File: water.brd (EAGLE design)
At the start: 100 x 80 mm, 15 parts, among them K1 AQH2223, K2 AQH2223, K3 AQH2223, K4 AQH2223, X5 MKDSN1,5/2-5,08, X6 MKDSN1,5/2-5,08, X7 MKDSN1,5/2-5,08, X8 MKDSN1,5/2-5,08

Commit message: Changes
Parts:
- moved X8 77.9 mm to (42.7, 46.3)
- moved D1 76.8 mm to (8.63, 46.0)
- moved X5 67.6 mm to (18.4, 38.1)
- moved X7 54.1 mm to (33.7, 37.3)
- moved K2 4.12 mm to (44.3, 23.9)
- moved K3 4.12 mm to (44.3, 9.16)
- moved U2 3.16 mm to (11.0, 14.2)
- moved K1 2.24 mm to (33.6, 23.9)
- moved K4 2.24 mm to (33.6, 9.16)
- moved R1 2.00 mm to (24.7, 14.0)
- moved R2 2.00 mm to (24.7, 10.2)
- moved R3 2.00 mm to (24.7, 3.81)
- moved R4 2.00 mm to (24.7, 19.1)
- moved X6 1.41 mm to (29.5, 46.0)
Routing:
- net GND: track 0.00 -> 117.8 mm
- net N$9: track 0.00 -> 37.6 mm
- net N$10: track 0.00 -> 36.3 mm
- net +3V3: track 0.00 -> 34.4 mm, vias 0 -> 1
- net N$8: track 0.00 -> 27.5 mm
- net N$15: track 0.00 -> 25.8 mm
- net N$2: track 0.00 -> 19.4 mm
- net N$3: track 0.00 -> 19.0 mm
- net N$11: track 0.00 -> 13.5 mm
- net N$12: track 0.00 -> 11.2 mm
- net N$14: track 0.00 -> 10.6 mm
- net N$1: track 0.00 -> 7.11 mm
- net N$4: track 0.00 -> 6.83 mm
- net N$5: track 0.00 -> 5.42 mm
- net N$7: track 0.00 -> 4.23 mm
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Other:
- board size 100 x 80 mm -> 62.7 x 68 mm

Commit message: Move parts
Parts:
- added SV2: (no value), con-lstb:MA04-2
- R1, R2, R3, R4: value 220 -> (none)
- moved D1 15.8 mm to (21.6, 37.0)
- moved X5 13.3 mm to (7.00, 45.0)
- moved K3 12.4 mm to (32.0, 7.00)
- moved X6 10.5 mm to (19.0, 45.0)
- moved K4 9.68 mm to (43.0, 7.00)
- moved X7 8.16 mm to (31.0, 45.0)
- moved K1 5.10 mm to (32.0, 19.0)
- moved K2 5.02 mm to (43.0, 19.0)
- moved SV1 3.16 mm to (3.35, 34.6), turned to 270 degrees
- moved X8 1.32 mm to (43.0, 45.0)
- moved R1 1.23 mm to (24.0, 15.0)
- moved R4 1.16 mm to (24.0, 20.0)
- moved R3 0.70 mm to (24.0, 4.00)
- moved R2 0.69 mm to (24.0, 10.0)
- moved U2 0.24 mm to (11.0, 14.0)
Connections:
- new net N$13: SV2.8, U2.CH_PD
- new net N$16: SV2.6, U2.RESET
- new net N$17: SV2.3, U2.TXD0
- new net N$18: SV2.1, U2.RXD0
- new net N$19: SV2.4, U2.GPIO15
- new net N$20: SV2.2, U2.GPIO0
- net +3V3: now also SV2.7
- net GND: now also SV2.5
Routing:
- net GND: track 117.8 -> 0.00 mm
- net N$9: track 37.6 -> 0.00 mm
- net N$10: track 36.3 -> 0.00 mm
- net +3V3: track 34.4 -> 0.00 mm, vias 1 -> 0
- net N$8: track 27.5 -> 0.00 mm
- net N$15: track 25.8 -> 0.00 mm
- net N$2: track 19.4 -> 0.00 mm
- net N$3: track 19.0 -> 0.00 mm
- net N$11: track 13.5 -> 0.00 mm
- net N$12: track 11.2 -> 0.00 mm
- net N$14: track 10.6 -> 0.00 mm
- net N$1: track 7.11 -> 0.00 mm
- net N$4: track 6.83 -> 0.00 mm
- net N$5: track 5.42 -> 0.00 mm
- net N$7: track 4.23 -> 0.00 mm
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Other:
- board size 62.7 x 68 mm -> 50 x 50 mm

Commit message: Restart routing
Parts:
- moved K1 1.00 mm to (32.0, 20.0)
- moved K2 1.00 mm to (43.0, 20.0)
- moved K3 1.00 mm to (32.0, 8.00)
- moved K4 1.00 mm to (43.0, 8.00)
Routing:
- net GND: track 0.00 -> 81.4 mm
- net N$10: track 0.00 -> 51.0 mm
- net N$12: track 0.00 -> 47.0 mm
- net N$9: track 0.00 -> 37.8 mm
- net N$11: track 0.00 -> 33.2 mm
- net N$4: track 0.00 -> 19.9 mm
- net N$2: track 0.00 -> 18.5 mm
- net N$3: track 0.00 -> 8.93 mm
- net N$1: track 0.00 -> 7.52 mm
- net N$5: track 0.00 -> 6.64 mm
- net N$6: track 0.00 -> 3.98 mm
- net N$7: track 0.00 -> 3.56 mm

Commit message: Changes
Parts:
- added C1, C2: 470uf, resistor:E5-10,5
- moved SV1 34.0 mm to (37.4, 34.6), turned to 90 degrees
- moved D1 20.2 mm to (41.6, 34.0), turned to 90 degrees
- moved SV2 6.00 mm to (5.00, 35.0)
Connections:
- new net N$21: K1.8, K2.8, K3.8, K4.8, X5.1
- net +3V3: now also C1.+, C2.+
- net GND: now also C1.-, C2.-; no longer K1.8, K2.8, K3.8, K4.8, X5.1
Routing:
- net N$21: track 0.00 -> 112.7 mm
- net +3V3: track 0.00 -> 66.9 mm
- net GND: track 81.4 -> 122.8 mm
- net N$15: track 0.00 -> 34.6 mm
- net N$18: track 0.00 -> 20.7 mm
- net N$17: track 0.00 -> 20.4 mm
- net N$14: track 0.00 -> 5.55 mm

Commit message: Changes
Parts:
- added LED1, LED2, LED3: X42180, led:Z-POWER-LED-DOME-TYPE
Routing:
- net N$19: track 0.00 -> 33.6 mm
- net N$13: track 0.00 -> 26.7 mm
- net N$20: track 0.00 -> 26.1 mm
- net N$8: track 0.00 -> 21.5 mm
- net N$16: track 0.00 -> 17.5 mm
- net N$18: track 20.7 -> 19.0 mm
- net N$17: track 20.4 -> 19.3 mm
- net +3V3: track 66.9 -> 66.7 mm, vias 0 -> 1
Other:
- board text added: "Sebastian Boyd"
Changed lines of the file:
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@@
 <wire x1="50" y1="50" x2="0" y2="50" width="0" layer="20"/>
 <wire x1="0" y1="50" x2="0" y2="0" width="0" layer="20"/>
+<text x="48" y="2" size="1.778" layer="16" rot="MR0">Sebastian Boyd</text>
 </plain>
 <attributes>
@@
 <element name="C1" library="resistor" library_urn="urn:adsk.eagle:library:348" package="E5-10,5" value="470uf" x="28" y="35" rot="R270"/>
 <element name="C2" library="resistor" library_urn="urn:adsk.eagle:library:348" package="E5-10,5" value="470uf" x="16" y="35" rot="R270"/>
+<element name="LED1" library="led" library_urn="urn:adsk.eagle:library:259" package="Z-POWER-LED-DOME-TYPE" value="X42180" x="7" y="-9"/>
+<element name="LED2" library="led" library_urn="urn:adsk.eagle:library:259" package="Z-POWER-LED-DOME-TYPE" value="X42180" x="7" y="-22"/>
+<element name="LED3" library="led" library_urn="urn:adsk.eagle:library:259" package="Z-POWER-LED-DOME-TYPE" value="X42180" x="7" y="-35"/>
 </elements>
 <signals>
@@
 <contactref element="U2" pad="GPIO13"/>
 <contactref element="R3" pad="1"/>
-<wire x1="2.7" y1="7.8" x2="22.578" y2="4" width="0" layer="19" extent="1-1"/>
+<wire x1="18.288" y1="4.1148" x2="22.5552" y2="4.1148" width="0.1524" layer="1"/>
+<wire x1="14.6304" y1="7.7724" x2="18.288" y2="4.1148" width="0.1524" layer="1"/>
+<wire x1="2.7432" y1="7.7724" x2="14.6304" y2="7.7724" width="0.1524" layer="1"/>
+<wire x1="22.5552" y1="4.1148" x2="22.578" y2="4" width="0.1524" layer="1"/>
+<wire x1="2.7432" y1="7.7724" x2="2.7" y2="7.8" width="0.1524" layer="1"/>
 </signal>
 <signal name="N$9">
@@
 <wire x1="16" y1="37.54" x2="7.54" y2="37.54" width="0.4064" layer="1"/>
 <wire x1="6.27" y1="38.81" x2="7.54" y2="37.54" width="0.4064" layer="1"/>
-<wire x1="2.7" y1="5.8" x2="3.8" y2="5.8" width="0.1524" layer="1"/>
-<wire x1="3.8" y1="5.8" x2="5" y2="7" width="0.1524" layer="1"/>
-<wire x1="5" y1="7" x2="5" y2="37.54" width="0.1524" layer="1"/>
-<wire x1="5" y1="37.54" x2="6.27" y2="38.81" width="0.1524" layer="1"/>
+<wire x1="3.5052" y1="5.9436" x2="2.7432" y2="5.9436" width="0.1524" layer="1"/>
+<wire x1="4.7244" y1="7.1628" x2="3.5052" y2="5.9436" width="0.1524" layer="1"/>
+<wire x1="4.7244" y1="37.1856" x2="4.7244" y2="7.1628" width="0.1524" layer="16"/>
+<wire x1="6.2484" y1="38.7096" x2="4.7244" y2="37.1856" width="0.1524" layer="16"/>
+<wire x1="2.7432" y1="5.9436" x2="2.7" y2="5.8" width="0.1524" layer="1"/>
+<wire x1="6.2484" y1="38.7096" x2="6.27" y2="38.81" width="0.1524" layer="16"/>
+<via x="4.7244" y="7.1628" extent="1-16" drill="0.3048"/>
 </signal>
 <signal name="N$15">
@@
 <contactref element="SV2" pad="8"/>
 <contactref element="U2" pad="CH_PD"/>
-<wire x1="2.7" y1="15.8" x2="3.73" y2="38.81" width="0" layer="19" extent="1-1"/>
+<wire x1="3.2004" y1="15.8496" x2="2.7432" y2="15.8496" width="0.1524" layer="1"/>
+<wire x1="4.572" y1="17.2212" x2="3.2004" y2="15.8496" width="0.1524" layer="1"/>
+<wire x1="4.572" y1="28.3464" x2="4.572" y2="17.2212" width="0.1524" layer="1"/>
+<wire x1="2.286" y1="30.6324" x2="4.572" y2="28.3464" width="0.1524" layer="1"/>
+<wire x1="2.286" y1="33.8328" x2="2.286" y2="30.6324" width="0.1524" layer="1"/>
+<wire x1="3.6576" y1="35.2044" x2="2.286" y2="33.8328" width="0.1524" layer="1"/>
+<wire x1="4.1148" y1="35.2044" x2="3.6576" y2="35.2044" width="0.1524" layer="1"/>
+<wire x1="4.7244" y1="35.814" x2="4.1148" y2="35.2044" width="0.1524" layer="1"/>
+<wire x1="4.7244" y1="37.7952" x2="4.7244" y2="35.814" width="0.1524" layer="1"/>
+<wire x1="3.81" y1="38.7096" x2="4.7244" y2="37.7952" width="0.1524" layer="1"/>
+<wire x1="2.7432" y1="15.8496" x2="2.7" y2="15.8" width="0.1524" layer="1"/>
+<wire x1="3.81" y1="38.7096" x2="3.73" y2="38.81" width="0.1524" layer="1"/>
 </signal>
 <signal name="N$16">
 <contactref element="U2" pad="RESET"/>
 <contactref element="SV2" pad="6"/>
-<wire x1="2.7" y1="19.8" x2="3.73" y2="36.27" width="0" layer="19" extent="1-1"/>
+<wire x1="2.5908" y1="29.8704" x2="2.5908" y2="19.812" width="0.1524" layer="1"/>
+<wire x1="1.9812" y1="30.48" x2="2.5908" y2="29.8704" width="0.1524" layer="1"/>
+<wire x1="1.9812" y1="34.4424" x2="1.9812" y2="30.48" width="0.1524" layer="1"/>
+<wire x1="3.6576" y1="36.1188" x2="1.9812" y2="34.4424" width="0.1524" layer="1"/>
+<wire x1="2.5908" y1="19.812" x2="2.7" y2="19.8" width="0.1524" layer="1"/>
+<wire x1="3.6576" y1="36.1188" x2="3.73" y2="36.27" width="0.1524" layer="1"/>
 </signal>
 <signal name="N$17">
 <contactref element="U2" pad="TXD0"/>
 <contactref element="SV2" pad="3"/>
-<wire x1="6.27" y1="33.73" x2="8.27" y2="33.73" width="0.1524" layer="1"/>
-<wire x1="8.27" y1="33.73" x2="19" y2="23" width="0.1524" layer="1"/>
-<wire x1="19" y1="23" x2="19" y2="19.9" width="0.1524" layer="1"/>
-<wire x1="19" y1="19.9" x2="19.1" y2="19.8" width="0.1524" layer="1"/>
+<wire x1="19.05" y1="21.0312" x2="19.05" y2="19.812" width="0.1524" layer="1"/>
+<wire x1="6.4008" y1="33.6804" x2="19.05" y2="21.0312" width="0.1524" layer="1"/>
+<wire x1="19.05" y1="19.812" x2="19.1" y2="19.8" width="0.1524" layer="1"/>
+<wire x1="6.4008" y1="33.6804" x2="6.27" y2="33.73" width="0.1524" layer="1"/>
 </signal>
 <signal name="N$18">
 <contactref element="U2" pad="RXD0"/>
 <contactref element="SV2" pad="1"/>
-<wire x1="6.27" y1="31.19" x2="8.81" y2="31.19" width="0.1524" layer="1"/>
-<wire x1="8.81" y1="31.19" x2="17" y2="23" width="0.1524" layer="1"/>
-<wire x1="17" y1="23" x2="17" y2="19" width="0.1524" layer="1"/>
-<wire x1="17" y1="19" x2="18" y2="18" width="0.1524" layer="1"/>
-<wire x1="18" y1="18" x2="18.9" y2="18" width="0.1524" layer="1"/>
-<wire x1="18.9" y1="18" x2="19.1" y2="17.8" width="0.1524" layer="1"/>
+<wire x1="18.5928" y1="17.8308" x2="19.05" y2="17.8308" width="0.1524" layer="1"/>
+<wire x1="6.4008" y1="30.0228" x2="18.5928" y2="17.8308" width="0.1524" layer="1"/>
+<wire x1="6.4008" y1="31.0896" x2="6.4008" y2="30.0228" width="0.1524" layer="1"/>
+<wire x1="19.05" y1="17.8308" x2="19.1" y2="17.8" width="0.1524" layer="1"/>
+<wire x1="6.4008" y1="31.0896" x2="6.27" y2="31.19" width="0.1524" layer="1"/>
 </signal>
 <signal name="N$19">
 <contactref element="SV2" pad="4"/>
 <contactref element="U2" pad="GPIO15"/>
-<wire x1="19.1" y1="7.8" x2="3.73" y2="33.73" width="0" layer="19" extent="1-1"/>
+<wire x1="18.4404" y1="7.9248" x2="19.05" y2="7.9248" width="0.1524" layer="1"/>
+<wire x1="4.8768" y1="21.4884" x2="18.4404" y2="7.9248" width="0.1524" layer="1"/>
+<wire x1="4.8768" y1="28.4988" x2="4.8768" y2="21.4884" width="0.1524" layer="1"/>
+<wire x1="2.5908" y1="30.7848" x2="4.8768" y2="28.4988" width="0.1524" layer="1"/>
+<wire x1="2.5908" y1="32.6136" x2="2.5908" y2="30.7848" width="0.1524" layer="1"/>
+<wire x1="3.6576" y1="33.6804" x2="2.5908" y2="32.6136" width="0.1524" layer="1"/>
+<wire x1="19.05" y1="7.9248" x2="19.1" y2="7.8" width="0.1524" layer="1"/>
+<wire x1="3.6576" y1="33.6804" x2="3.73" y2="33.73" width="0.1524" layer="1"/>
 </signal>
 <signal name="N$20">
 <contactref element="U2" pad="GPIO0"/>
 <contactref element="SV2" pad="2"/>
-<wire x1="19.1" y1="11.8" x2="3.73" y2="31.19" width="0" layer="19" extent="1-1"/>
+<wire x1="18.4404" y1="11.8872" x2="19.05" y2="11.8872" width="0.1524" layer="1"/>
+<wire x1="5.1816" y1="25.146" x2="18.4404" y2="11.8872" width="0.1524" layer="1"/>
+<wire x1="5.1816" y1="29.718" x2="5.1816" y2="25.146" width="0.1524" layer="1"/>
+<wire x1="3.81" y1="31.0896" x2="5.1816" y2="29.718" width="0.1524" layer="1"/>
+<wire x1="19.05" y1="11.8872" x2="19.1" y2="11.8" width="0.1524" layer="1"/>
+<wire x1="3.81" y1="31.0896" x2="3.73" y2="31.19" width="0.1524" layer="1"/>
 </signal>
 <signal name="N$21">

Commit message: Add led
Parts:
- removed LED2, LED3: X42180, led:Z-POWER-LED-DOME-TYPE
- added R5: (no value), resistor:R1206
- moved LED1 45.7 mm to (25.0, 33.0), flipped to the bottom
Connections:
- new net N$22: LED1.A, R5.1
- net +3V3: now also R5.2
- net GND: now also LED1.C
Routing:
- net +3V3: track 66.7 -> 77.6 mm
- net N$22: track 0.00 -> 7.30 mm
- net GND: track 122.8 -> 125.9 mm
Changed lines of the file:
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@@
 <element name="C1" library="resistor" library_urn="urn:adsk.eagle:library:348" package="E5-10,5" value="470uf" x="28" y="35" rot="R270"/>
 <element name="C2" library="resistor" library_urn="urn:adsk.eagle:library:348" package="E5-10,5" value="470uf" x="16" y="35" rot="R270"/>
-<element name="LED1" library="led" library_urn="urn:adsk.eagle:library:259" package="Z-POWER-LED-DOME-TYPE" value="X42180" x="7" y="-9"/>
-<element name="LED2" library="led" library_urn="urn:adsk.eagle:library:259" package="Z-POWER-LED-DOME-TYPE" value="X42180" x="7" y="-22"/>
-<element name="LED3" library="led" library_urn="urn:adsk.eagle:library:259" package="Z-POWER-LED-DOME-TYPE" value="X42180" x="7" y="-35"/>
+<element name="LED1" library="led" library_urn="urn:adsk.eagle:library:259" package="Z-POWER-LED-DOME-TYPE" value="X42180" x="25" y="33" rot="MR0"/>
+<element name="R5" library="resistor" library_urn="urn:adsk.eagle:library:348" package="R1206" value="" x="37" y="28" rot="MR180"/>
 </elements>
 <signals>
@@
 <wire x1="24" y1="28.46" x2="28" y2="32.46" width="0.4064" layer="1"/>
 <wire x1="24" y1="18" x2="24" y2="28.46" width="0.4064" layer="1"/>
+<contactref element="LED1" pad="C"/>
+<wire x1="16.1444" y1="32.83443125" x2="16.1444" y2="32.6044" width="0.4064" layer="16"/>
+<wire x1="16.1444" y1="32.6044" x2="16" y2="32.46" width="0.4064" layer="16"/>
+<wire x1="18.35" y1="34.12" x2="17.42996875" y2="34.12" width="0.4064" layer="16"/>
+<wire x1="17.42996875" y1="34.12" x2="16.1444" y2="32.83443125" width="0.4064" layer="16"/>
 </signal>
 <signal name="N$5">
@@
 <wire x1="6.2484" y1="38.7096" x2="6.27" y2="38.81" width="0.1524" layer="16"/>
 <via x="4.7244" y="7.1628" extent="1-16" drill="0.3048"/>
+<contactref element="R5" pad="2"/>
+<wire x1="38.422" y1="28" x2="38.422" y2="29.422" width="0.4064" layer="16"/>
+<wire x1="38.422" y1="29.422" x2="40" y2="31" width="0.4064" layer="16"/>
+<wire x1="40" y1="31" x2="40" y2="34.45" width="0.4064" layer="16"/>
+<wire x1="40" y1="34.45" x2="37.35" y2="37.1" width="0.4064" layer="16"/>
 </signal>
 <signal name="N$15">
@@
 <wire x1="29.1996" y1="17.26219375" x2="28.19" y2="18.27179375" width="0.4064" layer="16"/>
 </signal>
+<signal name="N$22">
+<contactref element="LED1" pad="A"/>
+<contactref element="R5" pad="1"/>
+<wire x1="31.65" y1="31.88" x2="34.12" y2="31.88" width="0.4064" layer="16"/>
+<wire x1="34.12" y1="31.88" x2="36" y2="30" width="0.4064" layer="16"/>
+<wire x1="36" y1="30" x2="36" y2="28.422" width="0.4064" layer="16"/>
+<wire x1="36" y1="28.422" x2="35.578" y2="28" width="0.4064" layer="16"/>
+</signal>
 </signals>

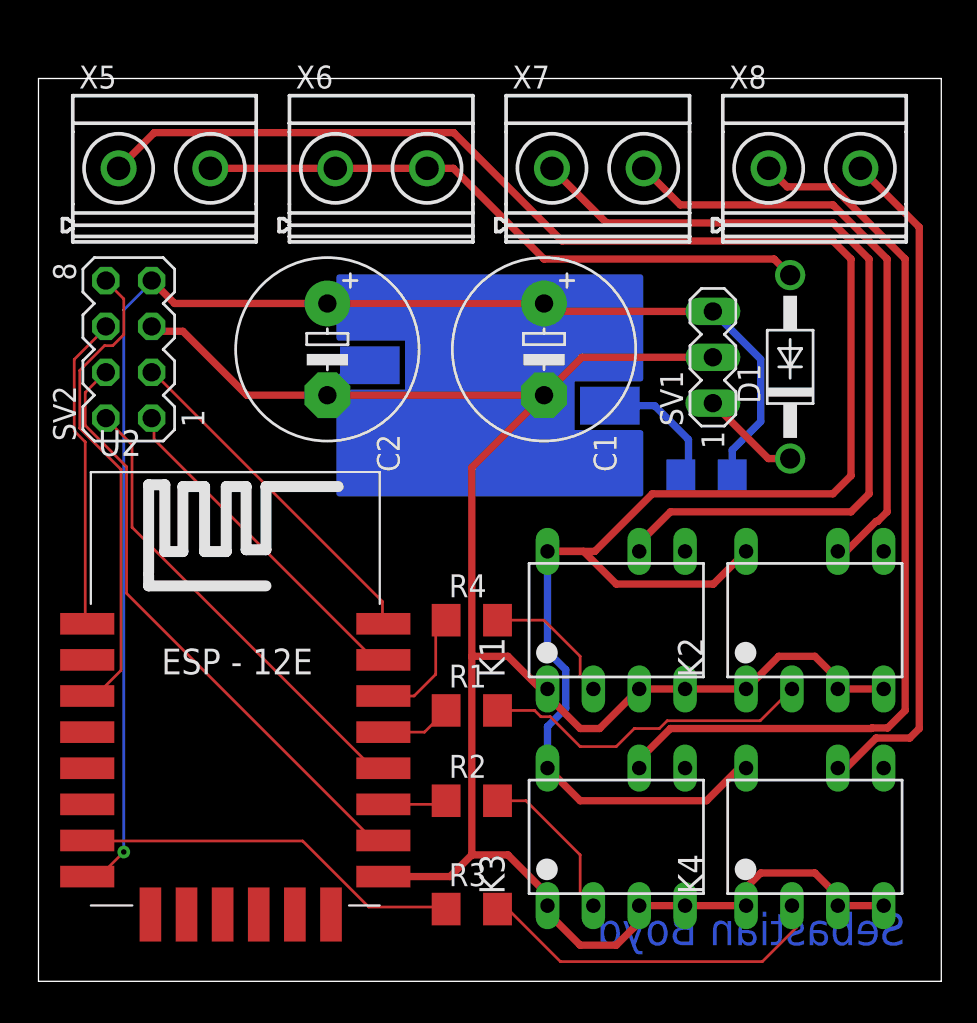
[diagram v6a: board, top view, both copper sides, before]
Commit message: Add pogo test bed
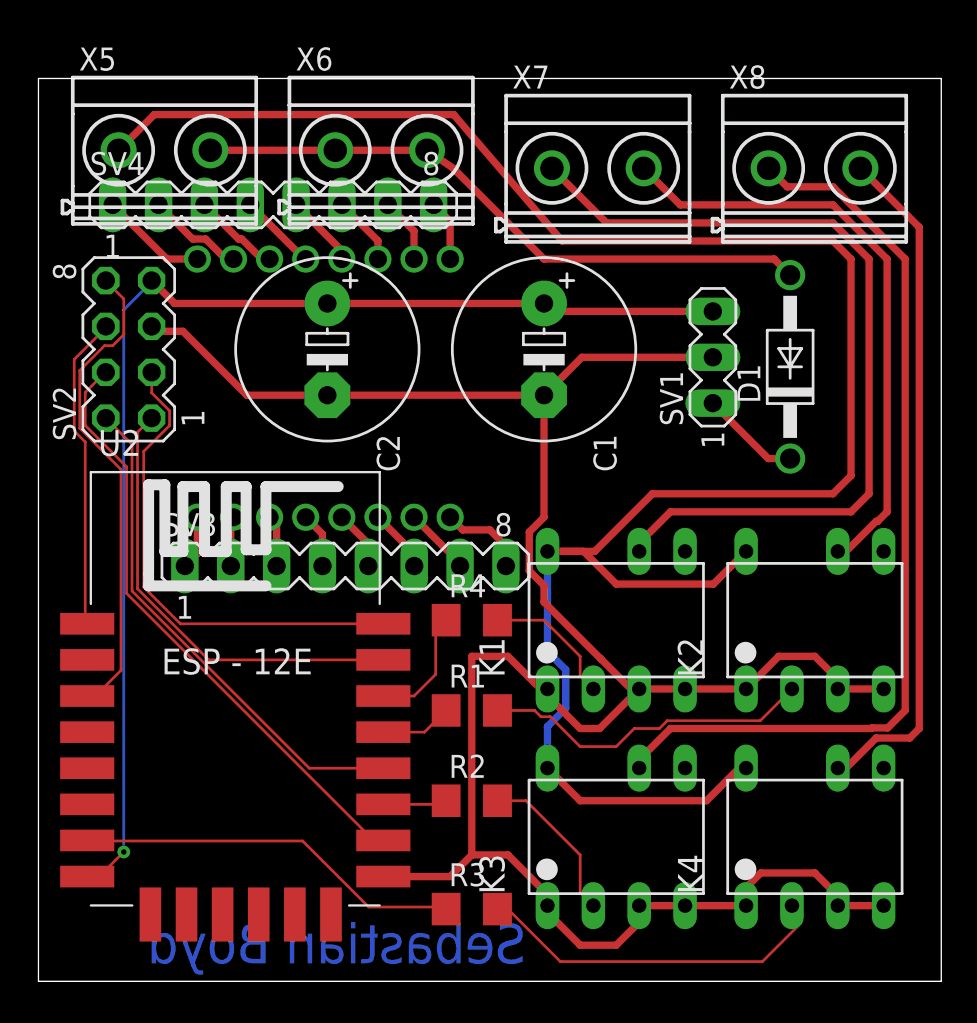
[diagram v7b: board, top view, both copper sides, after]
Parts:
- removed LED1: X42180, led:Z-POWER-LED-DOME-TYPE
- removed R5: (no value), resistor:R1206
- added SV3, SV4: (no value), con-lstb:MA08-1
- added U1: (no value), my-parts:ESP12E-POGO
- moved X5 1.00 mm to (7.00, 46.0)
- moved X6 1.00 mm to (19.0, 46.0)
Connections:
- new net N$23: SV3.2, U1.GPIO13
- new net N$24: SV3.3, U1.GPIO12
- new net N$25: SV3.4, U1.GPIO14
- new net N$26: SV3.5, U1.GPIO16
- new net N$27: SV3.6, U1.CH_PD
- new net N$28: SV3.7, U1.ADC
- new net N$29: SV3.8, U1.RESET
- new net N$30: SV4.1, U1.GND
- new net N$31: SV4.2, U1.GPIO15
- new net N$32: SV4.3, U1.GPIO2
- new net N$33: SV4.4, U1.GPIO0
- new net N$34: SV4.5, U1.GPIO4
- new net N$35: SV4.6, U1.GPIO5
- new net N$36: SV4.7, U1.RXD0
- new net N$37: SV4.8, U1.TXD0
- net +3V3: no longer R5.2
- net GND: no longer LED1.C
- net N$22: now also SV3.1, U1.VCC; no longer LED1.A, R5.1
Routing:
- net +3V3: track 77.6 -> 66.7 mm
- net N$17: track 19.3 -> 27.0 mm
- net N$18: track 19.0 -> 25.0 mm
- net N$30: track 0.00 -> 5.93 mm
- net N$31: track 0.00 -> 5.39 mm
- net N$29: track 0.00 -> 4.86 mm
- net N$32: track 0.00 -> 4.85 mm
- net N$22: track 7.30 -> 2.99 mm
- net N$33: track 0.00 -> 4.31 mm
- net N$34: track 0.00 -> 4.05 mm
- net N$35: track 0.00 -> 3.82 mm
- net N$28: track 0.00 -> 3.76 mm
- net N$36: track 0.00 -> 3.60 mm
- net N$27: track 0.00 -> 3.53 mm
- net N$37: track 0.00 -> 3.38 mm
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
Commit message: More features
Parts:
- removed SV1: (no value), con-lstb:MA03-1
- added D2: 1N4004, diode:DO41-10
- added SV5: (no value), my-parts:DC-DC
- moved D1 6.00 mm to (35.6, 34.0)
- moved X7 1.00 mm to (31.0, 46.0)
- moved X8 1.00 mm to (43.0, 46.0)
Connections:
- net +3V3: now also SV5.VO; no longer SV1.3
- net GND: now also D2.A, SV5.GND; no longer SV1.2
- net N$14: now also SV5.V1; no longer SV1.1
- net N$21: now also D2.C
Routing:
- net GND: track 126.1 -> 141.6 mm
- net N$14: track 5.55 -> 17.0 mm
- net N$21: track 113.4 -> 120.0 mm
- net +3V3: track 66.7 -> 72.8 mm
- net N$15: track 34.9 -> 28.9 mm
- net N$10: track 51.0 -> 51.8 mm
- net N$11: track 33.2 -> 34.0 mm
- net N$12: track 47.0 -> 47.7 mm
- net N$9: track 37.8 -> 38.5 mm
